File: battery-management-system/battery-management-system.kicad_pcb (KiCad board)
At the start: 4 copper layers, 147 x 100 mm, 200 parts, among them J1 CELL4_PLUS, J10 VBAT+_CHARGE, J11 I2C, J12 MCU_SUPPLY, J13 LEDS, J14 -5V, J15 TEMP_CELL1, J16 TEMP_CELL2, J17 TEMP_CELL3, J18 TEMP_CELL4, J19 CHARGE/DISCHARGE, J2 CELL4_MINUS, J20 UART_INTERCONNECT, J21 UART_USB, J22 BALANCE_INPUTS, J23 BALANCE_CURRENT, J24 3V3, J25 5V, J26 18V, J27 BALANCE_CONTROL, J28 9V4, J3 CELL3_MINUS, J4 CELL2_MINUS, J5 CELL1_MINUS, J6 VBAT+, J7 AMPHENOL_micro_usb_10118194-0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, J8 VBAT-, J9 rspro_header_5pin_3_5mm, Q1 DMN3730U, Q10 DMN3730U, Q11 DMN3404L, Q12 DMN3730U, Q14 DMN3730U, Q15 DMN3730U, Q16 DMN3730U, Q17 DMN3730U, Q2 TJ40S04M3L, Q3 TJ40S04M3L, Q4 DMN3730U, Q5 DMN3730U, Q6 BS250FTA, Q7 BS250FTA, Q8 BS250FTA, Q9 BS250FTA, SW1 CELL1_MINUS, SW2 CELL1_PLUS, SW3 CELL2_MINUS, SW4 CELL2_PLUS, SW5 CELL3_PLUS, SW6 CELL3_MINUS, SW7 CELL4_PLUS, SW8 CELL4_MINUS, U1 L6982C33DR, U10 LM2904M8-13, U11 LM2904M8-13, U12 ICL7660, U13 MC74VHC139, U14 STC3100, U15 ICL7660, U16 ICL7660, U2 L6982C33DR, U3 FT230XS, U4 STM32L071CZTx, U5 ARM-JTAG-SWD, U6 LM2904M8-13, U7 LM2904M8-13, U8 AT24C512C, U9 NCT75DR2G

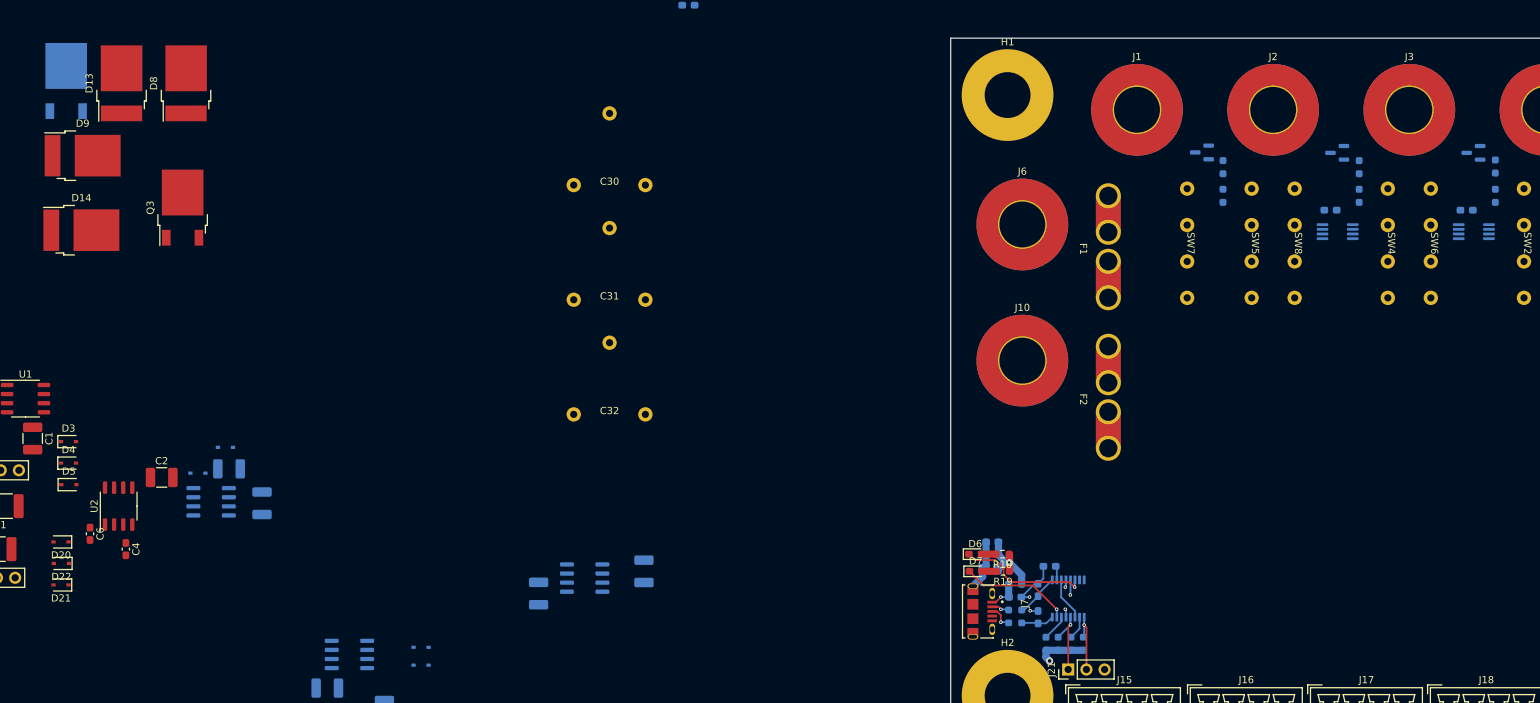
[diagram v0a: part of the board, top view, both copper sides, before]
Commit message: route power routes
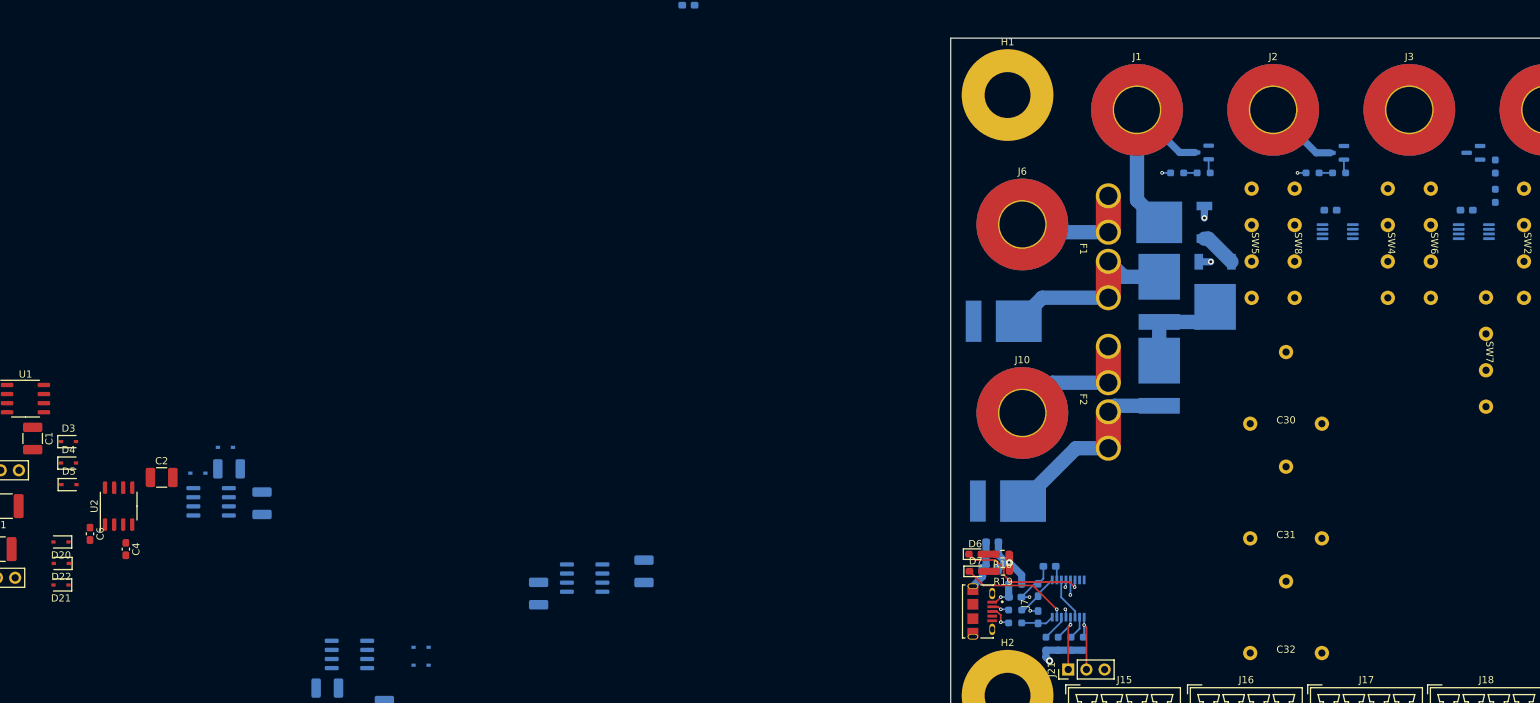
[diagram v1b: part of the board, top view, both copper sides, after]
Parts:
- D13, D14, D8, D9, Q3: moved to B.Cu
- moved Q2 155.9 mm to (51.2, 45.7), turned to 180 degrees
- moved D9 153.3 mm to (49.1, 67.1), turned to 90 degrees
- moved Q3 144.6 mm to (56.9, 55.4), turned to -90 degrees
- moved D8 138.9 mm to (49.1, 55.4)
- moved D14 134.7 mm to (28.0, 84.6)
- moved D13 127.5 mm to (27.4, 59.5), turned to 0 degrees
- moved C30 100.1 mm to (66.8, 73.8)
- moved C31 100.1 mm to (66.8, 89.8)
- moved C32 100.1 mm to (66.8, 105.8)
- moved SW7 44.4 mm to (94.7, 63.8)
- moved J10 7.30 mm to (30.0, 72.3)
- moved R27 7.24 mm to (70.5, 38.8), turned to 180 degrees
- moved R25 7.16 mm to (51.6, 38.8), turned to 180 degrees
- moved R26 2.91 mm to (74.2, 38.8), turned to 180 degrees
- moved R24 2.82 mm to (55.3, 38.8), turned to 180 degrees
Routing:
- net /Battery Pack/PACK: track 0.00 -> 29.7 mm
- net Net-(D14-K): track 0.00 -> 22.4 mm
- net Net-(D13-K): track 0.00 -> 21.9 mm
- net /PACK_EXT: track 0.00 -> 14.1 mm
- net Net-(J10-Pin_1): track 0.00 -> 13.7 mm
- net Net-(J6-Pin_1): track 0.00 -> 12.4 mm
- net /Battery Pack/CELL4_MINUS: track 0.00 -> 10.5 mm
- net Net-(Q2-S): track 0.00 -> 5.11 mm
- net GND: track 18.3 -> 20.7 mm, vias 4 -> 6
- net Net-(Q7-D): track 0.00 -> 2.28 mm
- net Net-(Q6-D): track 0.00 -> 1.99 mm
- net Net-(U6B-+): track 0.00 -> 1.88 mm
- net Net-(U6A-+): track 0.00 -> 1.88 mm
- net Net-(Q3-G): track 0.00 -> 1.68 mm, vias 0 -> 1
- net Net-(Q1-D): track 0.00 -> 1.68 mm, vias 0 -> 1

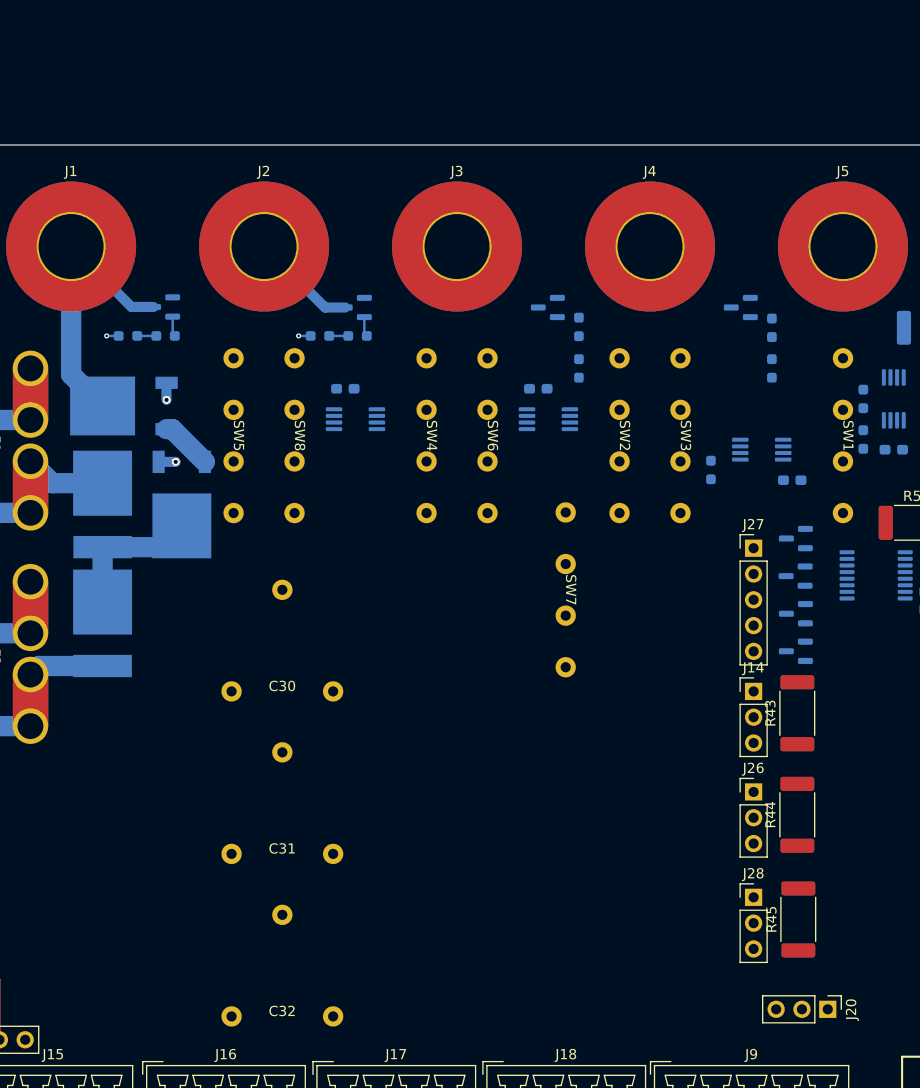
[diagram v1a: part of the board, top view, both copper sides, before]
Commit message: place balance caps and relais
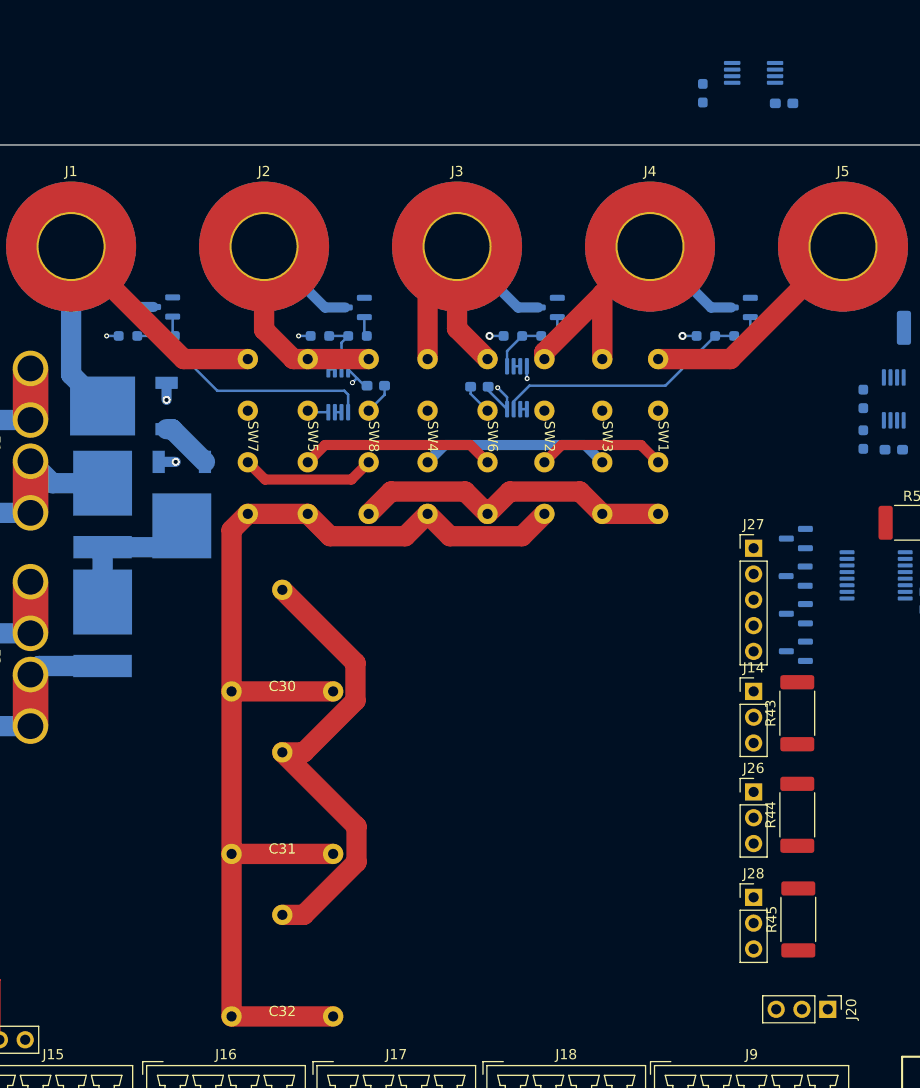
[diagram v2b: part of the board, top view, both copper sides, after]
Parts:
- moved C34 37.1 mm to (116.2, 15.9)
- moved R55 37.1 mm to (108.2, 14.9)
- moved U14 37.1 mm to (113.2, 12.9)
- moved SW7 34.8 mm to (63.4, 48.7)
- moved SW1 18.2 mm to (103.8, 48.7)
- moved SW3 7.70 mm to (98.3, 48.7)
- moved SW2 7.40 mm to (92.6, 48.7)
- moved SW5 7.30 mm to (69.3, 48.7)
- moved SW8 7.30 mm to (75.3, 48.7)
- moved R29 7.24 mm to (89.5, 38.8), turned to 180 degrees
- moved R31 7.24 mm to (108.5, 38.8), turned to 180 degrees
- moved C17 5.80 mm to (86.2, 43.8)
- moved U7 4.38 mm to (89.9, 43.9), turned to 90 degrees
- moved U6 3.28 mm to (72.3, 44.2), turned to -90 degrees
- moved C16 3.01 mm to (76.0, 43.7), turned to 180 degrees
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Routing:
- net /BALANCE_CAP_PLUS_RAW: track 0.00 -> 113.0 mm
- net /5V: track 0.00 -> 53.7 mm, vias 0 -> 1
- net /BALANCE_CAP_MINUS_RAW: track 0.00 -> 46.5 mm
- net /Battery Pack/CELL2_MINUS: track 0.00 -> 38.9 mm
- net /Battery Pack/CELL3_MINUS: track 0.00 -> 35.1 mm
- net Net-(Q11-S): track 0.00 -> 32.1 mm
- net Net-(U7A-+): track 0.00 -> 25.1 mm
- net /-5V: track 0.00 -> 23.1 mm, vias 0 -> 2
- net Net-(U6B-+): track 1.88 -> 24.9 mm
- net /Battery Pack/CELL1_MINUS: track 0.00 -> 22.8 mm
- net /Battery Pack/PACK: track 29.7 -> 51.7 mm
- net /Battery Pack/CELL4_MINUS: track 10.5 -> 30.2 mm
- net /Cell Balancing/CELL3: track 0.00 -> 19.1 mm
- net /Cell Balancing/CELL2: track 0.00 -> 18.6 mm
- net /Cell Balancing/CELL4: track 0.00 -> 13.3 mm
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
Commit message: work on layout
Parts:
- D1, D2, Q1, Q11, Q4, R2, R3, R43, R44, R45, R48, R54: moved to B.Cu
- moved R3 163.6 mm to (66.3, 51.1), turned to 180 degrees
- moved D2 162.6 mm to (67.4, 48.6), turned to -90 degrees
- moved Q1 161.3 mm to (60.2, 47.0), turned to -90 degrees
- moved R2 149.2 mm to (65.4, 47.9), turned to -90 degrees
- moved Q4 141.0 mm to (66.3, 53.8), turned to 180 degrees
- moved D1 139.2 mm to (65.6, 44.4), turned to 90 degrees
- moved R40 94.7 mm to (57.7, 63.1)
- moved U10 94.6 mm to (58.6, 68.4), turned to -90 degrees
- moved R39 94.5 mm to (59.6, 63.1)
- moved R41 91.0 mm to (63.3, 63.1), turned to -90 degrees
- moved C27 90.6 mm to (55.8, 69.9), turned to 90 degrees
- moved R42 87.8 mm to (61.4, 63.1), turned to 90 degrees
- moved R48 69.3 mm to (76.5, 65.6), turned to 180 degrees
- moved J23 43.6 mm to (91.9, 64.4), turned to 180 degrees
- moved R54 42.3 mm to (87.5, 64.0), turned to -90 degrees
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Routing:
- net /5V: track 53.7 -> 186.4 mm, vias 1 -> 3
- net /-5V: track 23.1 -> 124.6 mm, vias 2 -> 4
- net Net-(Q5-D): track 0.00 -> 78.5 mm
- net /BALANCE_CAP_MINUS_RAW: track 46.5 -> 103.9 mm
- net /MCU/SDA: track 0.00 -> 55.8 mm
- net /MCU/SCL: track 0.00 -> 55.8 mm
- net /Cell Measurement/BALANCE_CAP_PLUS: track 0.00 -> 48.9 mm
- net /CHARGE: track 0.00 -> 48.4 mm, vias 0 -> 1
- net /Cell Measurement/BALANCE_CAP_MINUS: track 0.00 -> 39.0 mm
- net /DISCHARGE: track 0.00 -> 37.9 mm
- net /Cell Measurement/CELL3: track 0.65 -> 35.2 mm, vias 0 -> 1
- net /Cell Measurement/CELL4: track 0.65 -> 34.3 mm
- net GND: track 23.4 -> 53.6 mm, vias 8 -> 15
- net /Cell Measurement/CELL2: track 0.65 -> 18.4 mm, vias 0 -> 1
- net /PACK_EXT: track 14.1 -> 28.8 mm, vias 0 -> 2
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
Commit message: work on layout
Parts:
- Q5, R22, R23: moved to B.Cu
- moved C36 358.0 mm to (275.9, 112.2)
- moved C5 358.0 mm to (240.6, 102.4)
- moved D15 358.0 mm to (271.5, 112.8)
- moved D20 358.0 mm to (252.4, 122.4)
- moved D21 358.0 mm to (252.4, 128.4)
- moved D23 358.0 mm to (275.4, 109.2)
- moved D5 358.0 mm to (253.5, 114.4)
- moved J25 358.0 mm to (240.9, 127.4)
- moved R9 358.0 mm to (232.5, 121.4)
- moved U15 358.0 mm to (273.4, 116.8)
- moved C1 358.0 mm to (248.4, 108.0)
- moved C2 358.0 mm to (266.4, 113.4)
- moved C3 358.0 mm to (240.4, 104.4)
- moved C37 358.0 mm to (280.4, 117.0)
- moved C4 358.0 mm to (261.4, 123.4)
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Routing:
- net /MCU/UART_USB_TX: track 9.86 -> 91.4 mm
- net /MCU/UART_USB_RX: track 9.17 -> 87.9 mm
- net /Cell Balancing/CELL4: track 13.3 -> 39.3 mm
- net /-5V: track 124.6 -> 149.2 mm, vias 4 -> 5
- net /PACK_EXT: track 28.8 -> 47.3 mm, vias 2 -> 3
- net GND: track 53.6 -> 71.4 mm, vias 15 -> 20
- net /Cell Balancing/CELL3: track 19.1 -> 33.6 mm
- net /18V: track 0.00 -> 14.4 mm
- net Net-(D25-K): track 0.00 -> 12.6 mm
- net Net-(J14-Pin_1): track 0.00 -> 11.7 mm
- net /5V: track 186.4 -> 196.6 mm, vias 3 -> 4
- net Net-(D24-K): track 0.00 -> 7.24 mm
- net Net-(U16-CAP+): track 0.00 -> 5.63 mm
- net /Cell Measurement/CELL1: track 15.1 -> 19.5 mm
- net /Cell Measurement/CELL3: track 35.2 -> 39.2 mm
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
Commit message: finish first draft of layout
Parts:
- removed H4: MountingHole_Pad, MountingHole:MountingHole_6.4mm_M6_Pad
- C1, C18, C19, C2, C20, C21, C22, C23, C24, C25, C26, C3, C4, C5, C6, C7, C8, D20, D21, D22, D3, D4, D5, FB2, Q10, Q12, R20, R21, R35, R36, R37, R38, R4, R46, R47, R49, R5, R50, R51, R52, R59, R6, R7, U1, U2, U4, U8, U9: moved to B.Cu
- moved D5 217.3 mm to (37.2, 93.7), turned to 180 degrees
- moved C1 210.0 mm to (39.2, 89.9), turned to 90 degrees
- moved C5 207.7 mm to (33.2, 90.2), turned to 90 degrees
- moved Q10 207.5 mm to (52.4, 88.2), turned to 180 degrees
- moved D3 207.3 mm to (47.5, 85.0), turned to 90 degrees
- moved R47 207.1 mm to (52.2, 90.9), turned to 180 degrees
- moved C18 205.9 mm to (52.8, 108.0), turned to 90 degrees
- moved R46 203.9 mm to (55.4, 88.2), turned to -90 degrees
- moved U1 202.7 mm to (44.9, 93.8), turned to 180 degrees
- moved J24 200.4 mm to (41.5, 99.1), turned to 0 degrees
- moved R51 197.8 mm to (46.0, 105.7), turned to 90 degrees
- moved C3 195.3 mm to (45.3, 97.7)
- moved U8 194.8 mm to (56.6, 106.0), turned to -90 degrees
- moved D22 194.4 mm to (64.1, 77.2), turned to -90 degrees
- moved L1 193.8 mm to (35.8, 89.9), turned to 180 degrees
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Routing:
- net GND: track 71.4 -> 215.5 mm, vias 20 -> 48
- net /5V_USB: track 12.9 -> 154.9 mm, vias 2 -> 3
- net Net-(D3-K): track 0.00 -> 120.0 mm, vias 0 -> 3
- net /MCU/SCL: track 55.8 -> 167.9 mm, vias 0 -> 1
- net /MCU/SDA: track 55.8 -> 167.0 mm, vias 0 -> 3
- net /Cell Measurement/CELL3: track 39.2 -> 116.9 mm, vias 1 -> 2
- net /Cell Measurement/CELL4: track 37.1 -> 114.5 mm, vias 0 -> 2
- net /Cell Measurement/CELL2: track 19.9 -> 94.1 mm, vias 1 -> 2
- net /MCU/SWDIO: track 0.00 -> 73.1 mm, vias 0 -> 4
- net /Cell Measurement/CELL1: track 19.5 -> 92.6 mm, vias 0 -> 2
- net /MCU/SWCLK: track 0.00 -> 70.0 mm, vias 0 -> 4
- net /Battery Pack/CHARGE_AVAILABLE: track 0.00 -> 66.2 mm, vias 0 -> 2
- net /MCU/NRST: track 0.00 -> 57.7 mm
- net /CHARGE: track 49.5 -> 104.6 mm, vias 1 -> 2
- net /5V: track 196.6 -> 250.2 mm, vias 4 -> 7
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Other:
- board size 147 x 100 mm -> 130 x 100 mm

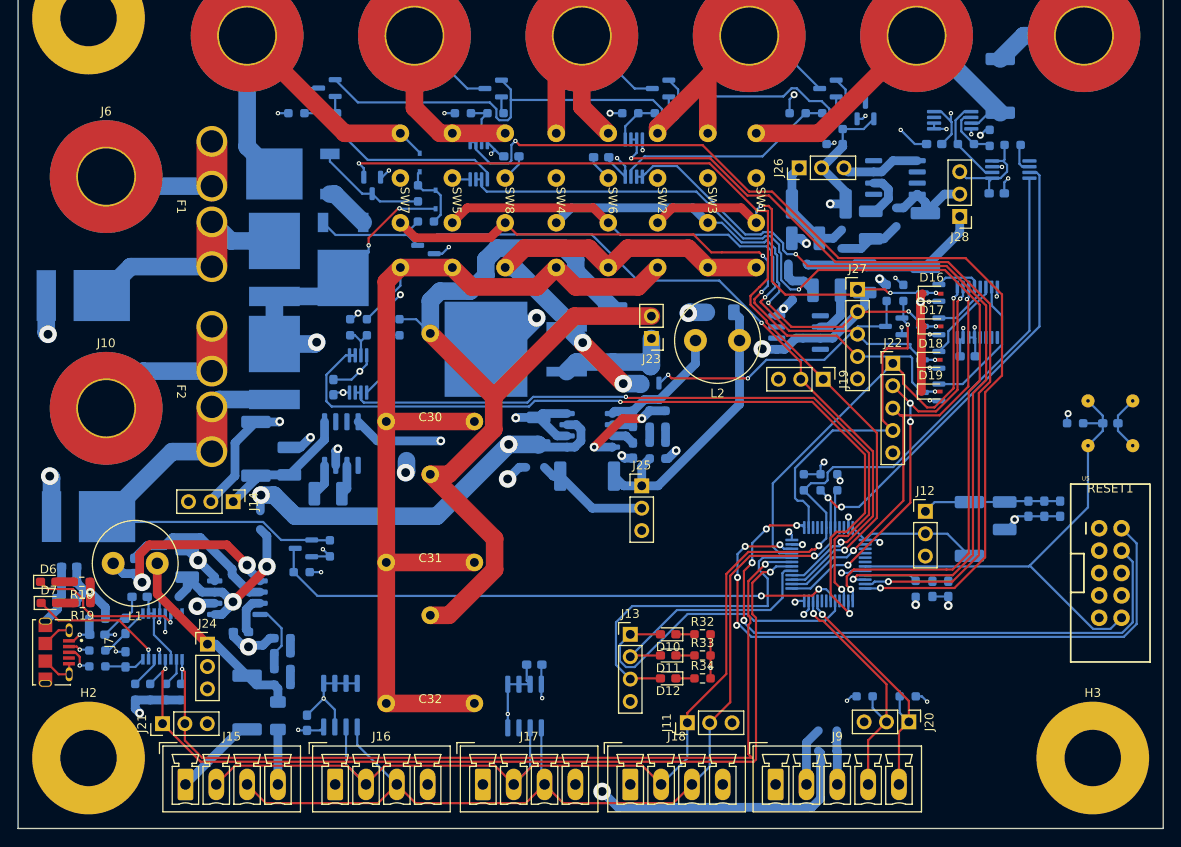
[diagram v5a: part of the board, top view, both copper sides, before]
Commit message: fix design rule errors
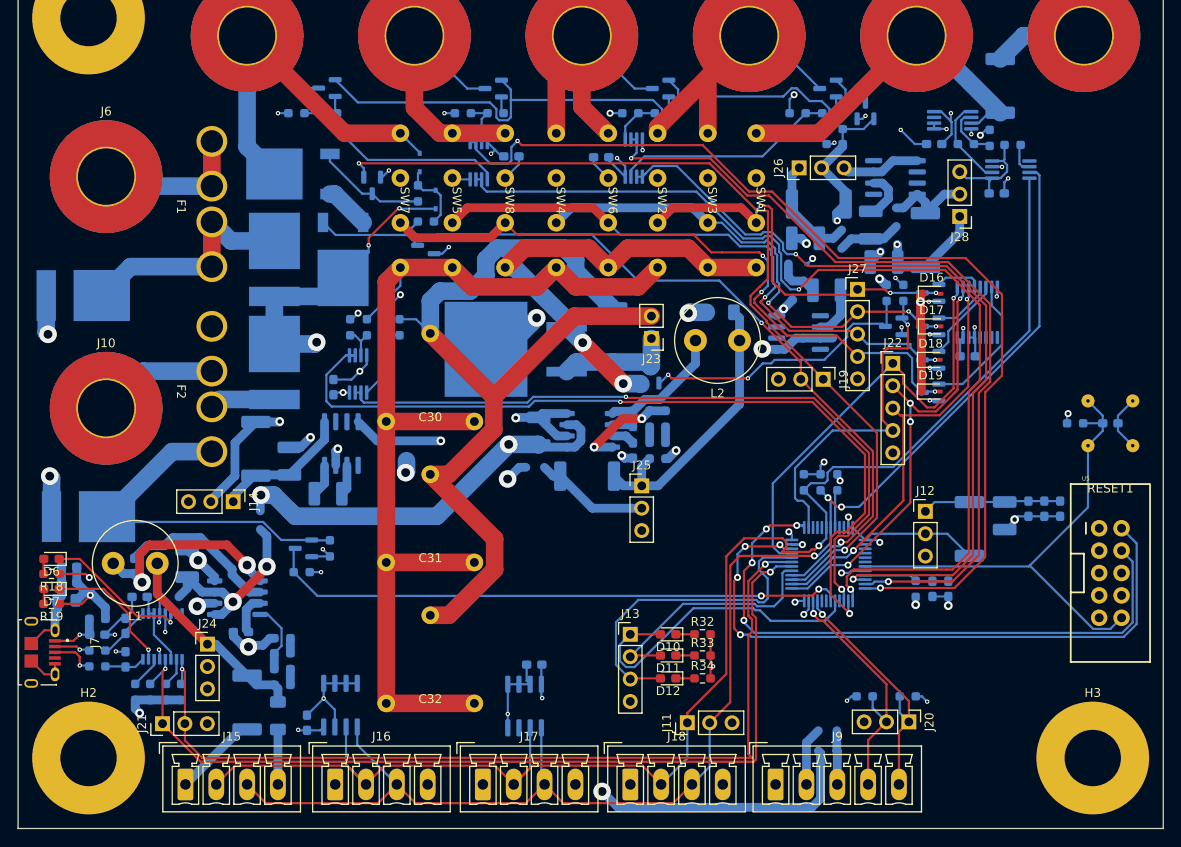
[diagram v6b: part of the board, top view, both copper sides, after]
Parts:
- moved R18 3.54 mm to (23.8, 91.1)
- moved R19 3.50 mm to (23.8, 94.5)
- moved C37 2.91 mm to (118.3, 55.7), turned to 180 degrees
- moved D6 2.63 mm to (23.8, 89.4), turned to 180 degrees
- moved D7 1.63 mm to (23.8, 92.8), turned to 180 degrees
- moved J7 1.60 mm to (21.5, 100.0)
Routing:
- net /5V_USB: track 154.9 -> 164.6 mm, vias 3 -> 4
- net /Power Supply/9V4: track 20.9 -> 29.0 mm, vias 0 -> 2
- net Net-(J6-Pin_1): track 12.4 -> 17.5 mm
- net Net-(D13-K): track 21.9 -> 26.9 mm
- net GND: track 215.5 -> 211.3 mm, vias 48 -> 49
- net /MCU/SCL: track 167.9 -> 171.7 mm
- net /5V: track 250.2 -> 253.8 mm
- net /18V: track 28.1 -> 26.3 mm
- net Net-(J7-D+): track 3.55 -> 5.15 mm
- net Net-(J7-VCC): track 4.47 -> 6.07 mm
- net Net-(J7-D-): track 2.50 -> 4.10 mm
- net Net-(D6-K): track 18.2 -> 16.6 mm
- net Net-(Q11-G): track 31.7 -> 32.4 mm
- net /MCU/SDA: track 167.0 -> 167.7 mm
- net /MCU/SWDIO: track 73.1 -> 73.7 mm
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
